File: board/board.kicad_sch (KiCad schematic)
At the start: 3 parts, among them J1 013_PoE_rectified, J2 014_PoE_controlled

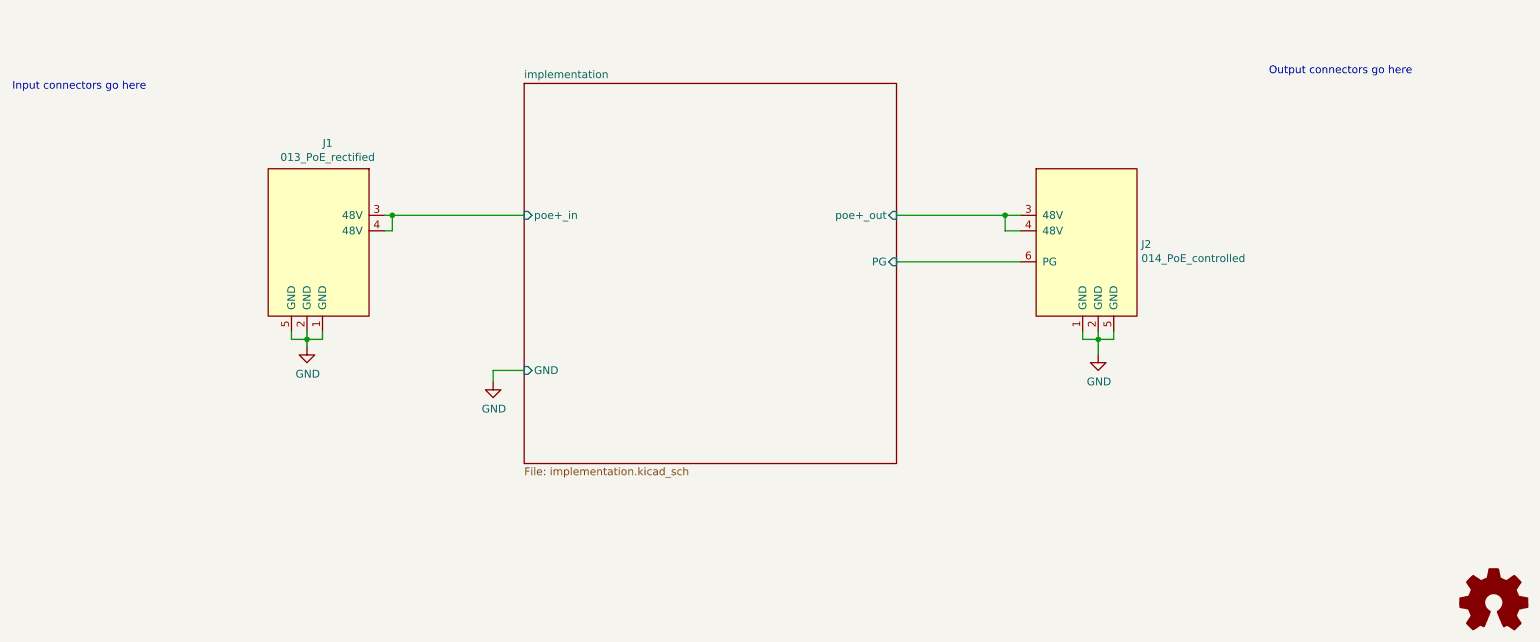
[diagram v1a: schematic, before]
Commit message: Moved Q1 from front to back
Q1 from front to back and keeped the size of pcb
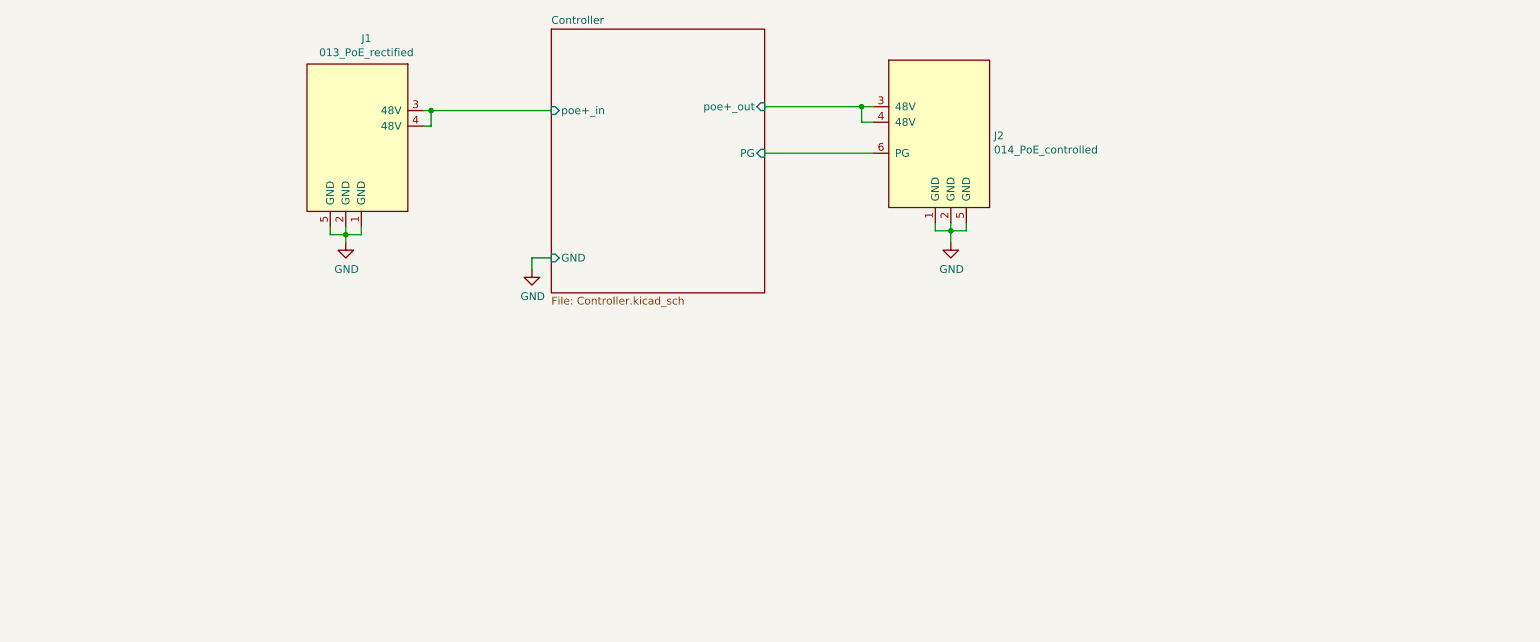
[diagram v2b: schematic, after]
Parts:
- removed J1: 013_PoE_rectified, on_edge:on_edge_2x05_device, symbol put_on_edge:013_PoE_rectified
- removed J2: 014_PoE_controlled, on_edge:on_edge_2x05_host, symbol put_on_edge:014_PoE_controlled
- removed LOGO1: Logo_Open_Hardware_Small, Symbol:OSHW-Symbol_6.7x6mm_SilkScreen, symbol Graphic:Logo_Open_Hardware_Small
- added J1: 013_PoE_rectified, on_edge:on_edge_2x05_device, symbol board-rescue:013_PoE_rectified-put_on_edge
- added J2: 014_PoE_controlled, on_edge:on_edge_2x05_host, symbol board-rescue:014_PoE_controlled-put_on_edge
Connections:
- net GND: now also J1.1 (GND), J1.2 (GND), J1.5 (GND), J2.1 (GND), J2.2 (GND), J2.5 (GND)
- new net Controller/PG: J2.6 (PG)
- new net Controller/poe+_in: J1.3 (48V), J1.4 (48V)
- new net Controller/poe+_out: J2.3 (48V), J2.4 (48V)
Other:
- removed sheet implementation
- added sheet Controller (Controller.kicad_sch)
- note removed: "Input connectors go here"
- note removed: "Output connectors go here"
